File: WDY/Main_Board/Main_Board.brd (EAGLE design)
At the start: 130 x 70 mm, 171 parts, among them J1 22-05-7028-02, J10 22-05-7038-03, J11 22-05-7028-02, J12 22-05-7028-02, J13 22-05-7028-02, J14 22-05-7028-02, J15 22-05-7038-03, J2 22-05-7028-02, J3 22-05-7048-04, J4 22-05-7048-04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

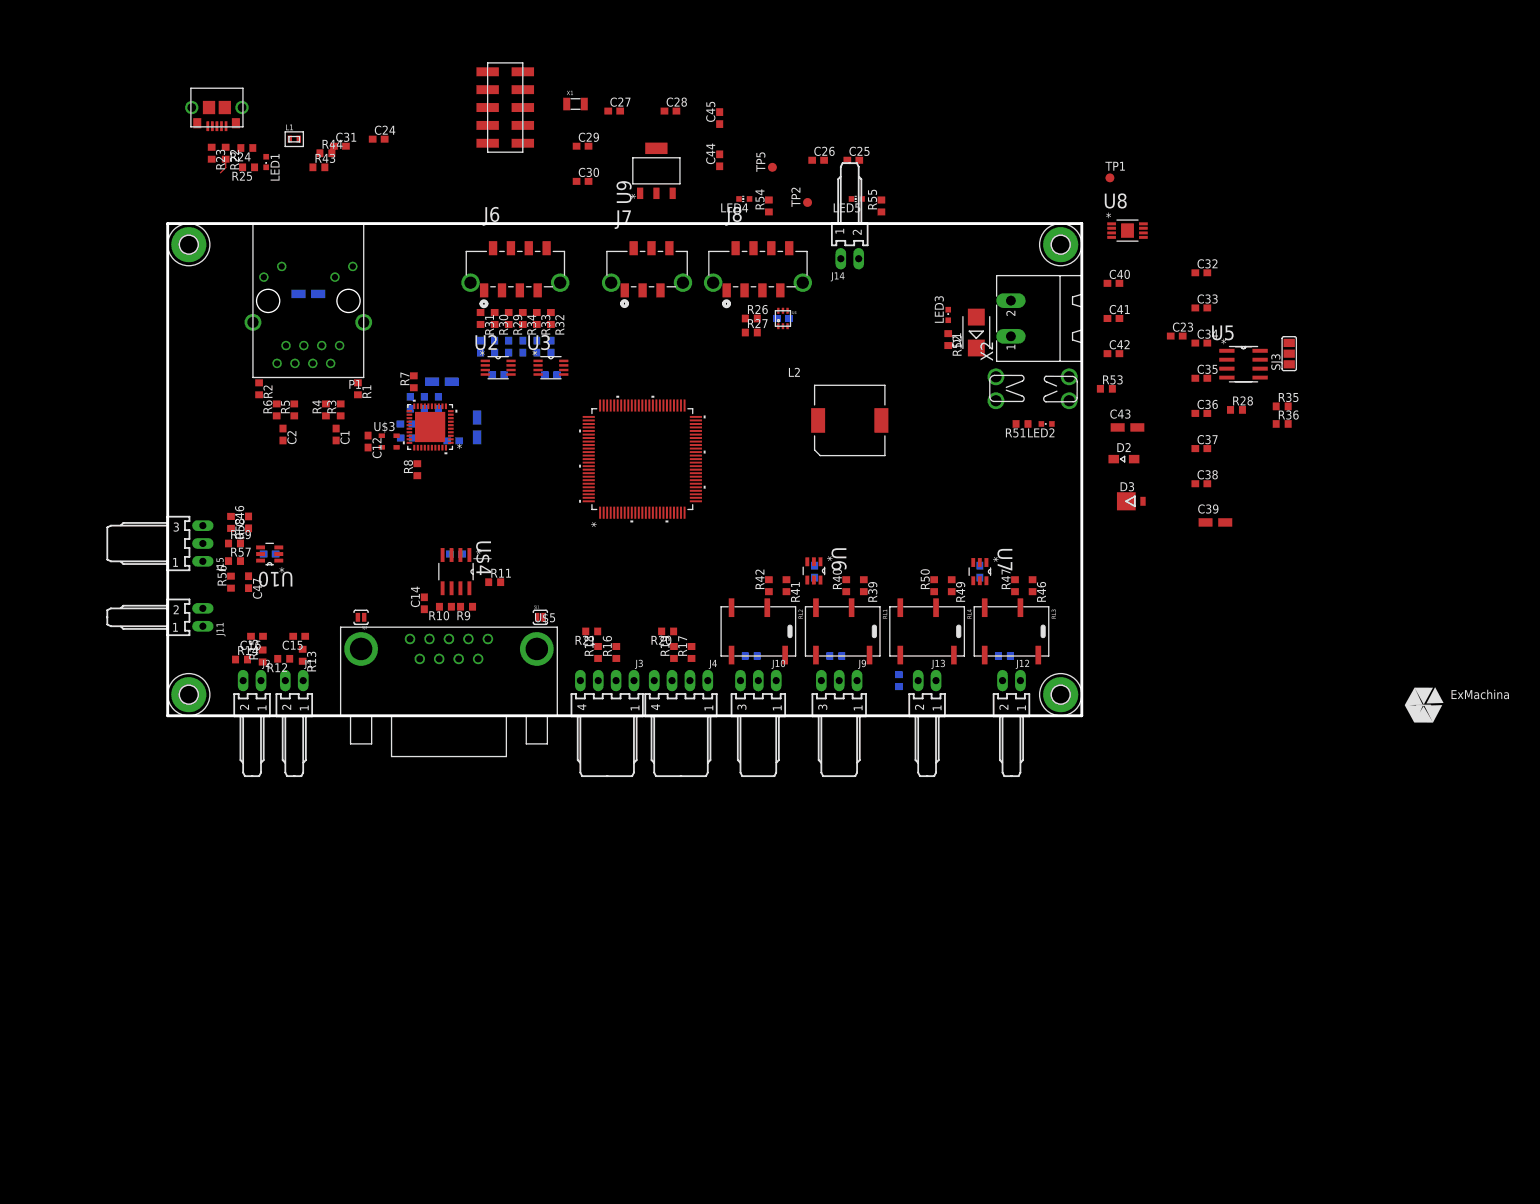
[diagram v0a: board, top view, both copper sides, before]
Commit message: Change relay to G6K Place components on the board
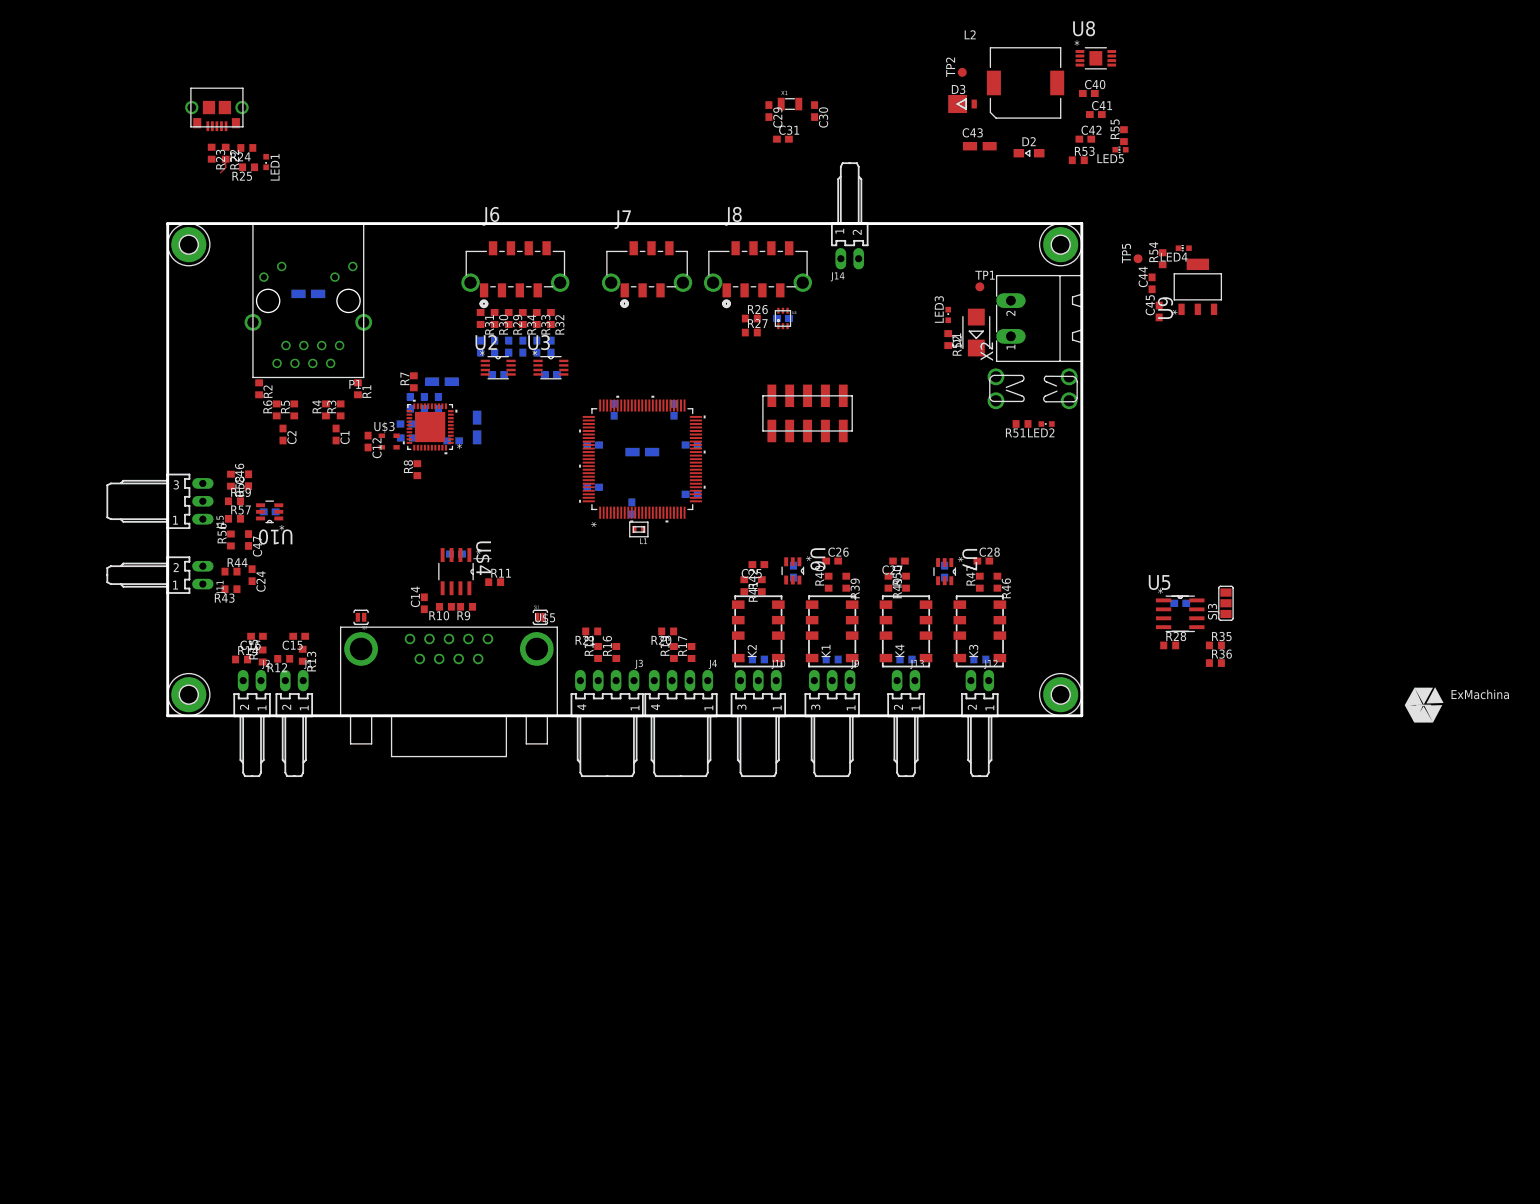
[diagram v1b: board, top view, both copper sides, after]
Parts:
- removed RL1, RL2, RL3, RL4: G6L24DC, rel-omron:G6L-1F
- added K1, K2, K3, K4: G6K-2G-Y, relay:G6K-2G-Y
- moved C33 90.2 mm to (60.5, 32.5), flipped to the bottom
- moved C32 87.7 mm to (66.0, 29.5), flipped to the bottom, turned to 90 degrees
- moved C38 86.7 mm to (60.5, 38.5), flipped to the bottom, turned to 180 degrees
- moved C37 83.7 mm to (63.5, 43.5), flipped to the bottom, turned to 270 degrees
- moved C39 82.1 mm to (67.5, 37.5), flipped to the bottom, turned to 180 degrees
- moved U9 78.7 mm to (146.5, 61.0)
- moved C28 78.0 mm to (116.0, 22.0)
- moved C27 75.7 mm to (104.0, 22.0), turned to 180 degrees
- moved C34 75.6 mm to (74.5, 31.5), flipped to the bottom
- moved C36 75.0 mm to (72.0, 43.5), flipped to the bottom, turned to 270 degrees
- moved L1 74.0 mm to (67.0, 26.5), turned to 180 degrees
- moved C35 73.1 mm to (74.5, 38.5), flipped to the bottom
- moved C45 68.3 mm to (141.0, 57.5)
- moved C24 64.6 mm to (12.0, 20.0), turned to 270 degrees
- moved C44 63.9 mm to (140.0, 61.5)
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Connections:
- removed net N$35: R48.2, RL4.5
- new net N$55: K2.1, R37.2
- new net N$57: K2.4, K2.6
- new net N$58: K1.5, R39.2, R40.1
- new net N$59: K4.4, K4.6
- new net N$60: K3.4, K3.6
- net GND: now also K1.3, K1.8, K2.3, K2.8, K3.3, K3.8, K4.3, K4.8; no longer RL1.4, RL1.8, RL2.4, RL2.8, RL3.4, RL3.8, RL4.4, RL4.8
- net N$24: now also K1.1; no longer RL1.5
- net N$28: now also K3.1, R45.2; no longer R37.2, RL2.5
- net N$29: now also K1.4, K1.6; no longer R39.2, R40.1, RL1.2
- net N$30: now also K2.5; no longer RL2.2
- net N$33: now also K4.1, R48.2; no longer R45.2, RL3.5
- net N$34: now also K3.5; no longer RL3.2
- net N$36: now also K4.5; no longer RL4.2

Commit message: Add Encoder channel Z
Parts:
- removed U10: SN74LVC2G17DBVR, ti:SOT95P280X145-6N
- added C54: 0.1uF, rcl:C0603
- added R60: 100, rcl:R0603
- added R61: 4k7, rcl:R0603
- added U11: SN74LVC3G17DCTR, ti:SOP65P400X130-8N
- J15: value 22-05-7038-03 -> 22-05-7058-05; device con-molex:7395-03 -> con-molex:7395-05
- moved J14 87.0 mm to (10.0, 65.0)
- moved J3 83.0 mm to (75.5, 87.0)
- moved J4 83.0 mm to (86.0, 87.0)
- moved R16 83.0 mm to (76.8, 91.0)
- moved R17 83.0 mm to (87.5, 91.0)
- moved R18 83.0 mm to (74.2, 91.0)
- moved R19 83.0 mm to (85.0, 91.0)
- moved R20 83.0 mm to (84.1, 94.0)
- moved R21 83.0 mm to (73.3, 94.0)
- moved R28 81.6 mm to (75.5, 56.5), turned to 90 degrees
- moved C29 63.0 mm to (22.5, 84.5)
- moved C30 63.0 mm to (29.0, 84.5)
- moved C31 63.0 mm to (24.5, 80.5)
- moved X1 63.0 mm to (25.5, 85.5)
- moved J15 62.1 mm to (-9.00, -30.0), turned to 0 degrees
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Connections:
- net N$40 renamed VIN
- new net ENCODER_Z: U1.65, U11.2
- new net N$35: J15.2, R56.2, R57.1
- new net N$40: J15.3, R59.1, R61.2
- new net N$62: J15.5
- net +3V3: now also U11.8; no longer U10.5
- net +5V: now also J15.1, R61.1
- net ENCODER_A: now also U1.67, U11.7; no longer U1.77, U10.1
- net ENCODER_B: now also U1.66, U11.5; no longer U1.76, U10.3
- net GND: now also C54.2, U11.4; no longer J15.3, U10.2
- net N$46: now also J15.4, R58.2, R60.1; no longer J15.1, R56.2, R57.1
- net N$52: now also C54.1, R60.2, U11.6; no longer J15.2, R58.2, R59.1
- net N$53: now also R59.2, U11.3; no longer R57.2, U10.6
- net N$54: now also R57.2, U11.1; no longer R59.2, U10.4
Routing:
- added copper zone on layer 1, net +24V
- added copper zone on layer 1, net VIN

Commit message: Power polygon on the board
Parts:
- moved C54 123.0 mm to (76.5, 10.5)
- moved R60 123.0 mm to (75.0, 20.5)
- moved R61 123.0 mm to (75.0, 15.5)
- moved U11 107.2 mm to (65.0, 19.0)
- moved R17 103.9 mm to (9.00, 23.0), turned to 0 degrees
- moved J4 102.3 mm to (5.00, 24.5), turned to 270 degrees
- moved R19 100.3 mm to (9.00, 25.5), turned to 0 degrees
- moved R20 98.8 mm to (12.0, 26.4), turned to 90 degrees
- moved R16 88.8 mm to (9.00, 33.7), turned to 0 degrees
- moved J3 87.6 mm to (5.00, 35.0), turned to 270 degrees
- moved R18 85.1 mm to (9.00, 36.3), turned to 0 degrees
- moved J15 84.1 mm to (67.5, 5.00)
- moved R21 83.6 mm to (12.0, 37.2), turned to 90 degrees
- moved R56 65.3 mm to (72.0, 8.00), turned to 180 degrees
- moved R57 62.6 mm to (69.0, 8.50), turned to 90 degrees
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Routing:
- added copper zone on layer 3, net +24V
- added copper zone on layer 3, net +5V
